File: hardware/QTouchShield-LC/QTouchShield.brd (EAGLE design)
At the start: 100 x 80 mm, 59 parts, among them IC1 AT32UC3C0512CJEDEC-MS-026, J1 SNS00...07, J10 CAPS08...15, J11 CAPS16...23, J12 CAPS24...31, J2 SNS08...15, J3 SNS16...23, J4 SNS24...31, J5 RES00...07, J6 RES08...15, J7 RES16...23, J8 RES24...31, J9 CAPS00...07, U1 ARDUINO-2560-MEGA-R3-SMD

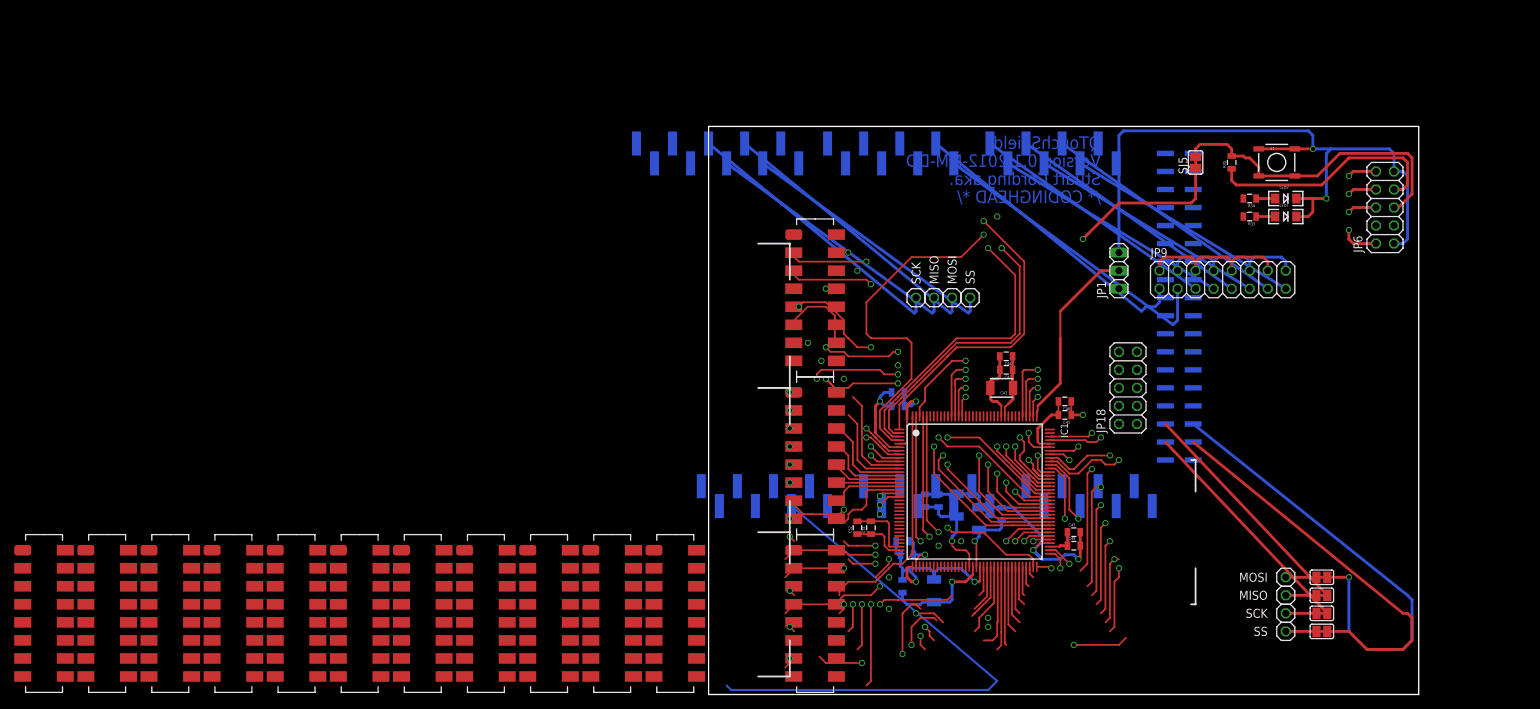
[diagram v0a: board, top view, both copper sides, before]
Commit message: Board ripped up - new surface mount headers fitted.
Ripped-up entire board. Most headers have been changed to surface mount
type.
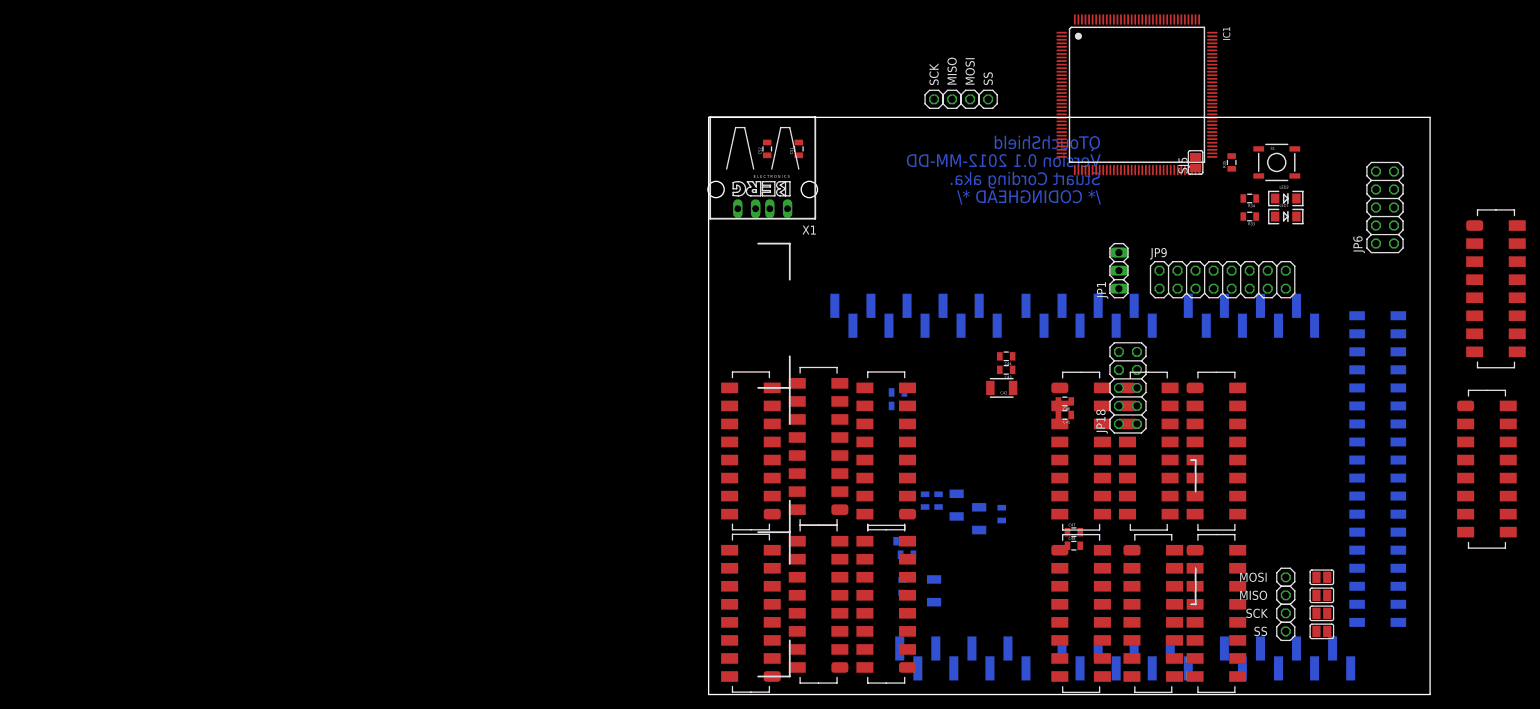
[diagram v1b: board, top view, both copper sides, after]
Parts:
- added X1: (no value), con-berg:PN87520
- moved J8 156.2 mm to (61.0, 20.3)
- moved J12 137.2 mm to (50.8, 20.3)
- moved U$2 132.6 mm to (109.2, 66.0)
- moved J11 130.3 mm to (50.8, 43.2)
- moved U$1 116.1 mm to (108.0, 40.6)
- moved J3 105.4 mm to (69.8, 43.2)
- moved J10 95.4 mm to (26.7, 25.4), turned to 180 degrees
- moved J4 94.0 mm to (69.8, 20.3)
- moved J9 87.9 mm to (26.7, 3.81), turned to 180 degrees
- moved J1 61.1 mm to (7.62, 2.54), turned to 180 degrees
- moved IC1 60.4 mm to (60.3, 84.5)
- moved C52 54.8 mm to (8.26, 76.8)
- moved C51 54.3 mm to (12.7, 76.8)
- moved J7 51.7 mm to (60.3, 43.2)
- moved J2 49.8 mm to (7.62, 25.4), turned to 180 degrees
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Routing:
- net GND: track 275.7 -> 0.00 mm, vias 7 -> 0
- net SDT-SPI0-SS: track 172.0 -> 0.00 mm, vias 1 -> 0
- net SDT-SPI0-MOSI: track 171.9 -> 0.00 mm, vias 2 -> 0
- net SDT-SPI0-SCK: track 150.4 -> 0.00 mm, vias 1 -> 0
- net SDT-SPI0-MISO: track 148.5 -> 0.00 mm, vias 1 -> 0
- net SNSK19: track 119.7 -> 0.00 mm, vias 5 -> 0
- net SNSK21: track 112.6 -> 0.00 mm, vias 3 -> 0
- net SNSK20: track 110.4 -> 0.00 mm, vias 4 -> 0
- net JTAG_RESET: track 109.4 -> 0.00 mm, vias 2 -> 0
- net JTAG_TCK: track 106.9 -> 0.00 mm, vias 2 -> 0
- net JTAG_TMS: track 105.9 -> 0.00 mm, vias 2 -> 0
- net JTAG_TDO: track 102.1 -> 0.00 mm, vias 3 -> 0
- net SNSK18: track 100.7 -> 0.00 mm, vias 4 -> 0
- net SNSK22: track 98.2 -> 0.00 mm, vias 5 -> 0
- net VCC: track 97.9 -> 0.00 mm, vias 5 -> 0
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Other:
- board size 100 x 80 mm -> 101.6 x 81.3 mm

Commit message: Major update to LC version of shield.
Major update to shield design including:
- Moving headers to surface mount technology
- Including level shifters for SPI and USART i/f
- USB connector for firmware flash upgrade (not yet complete)
- Jumper system for selecting MEGA or UNO style SPI interface
- Plus other tidying up
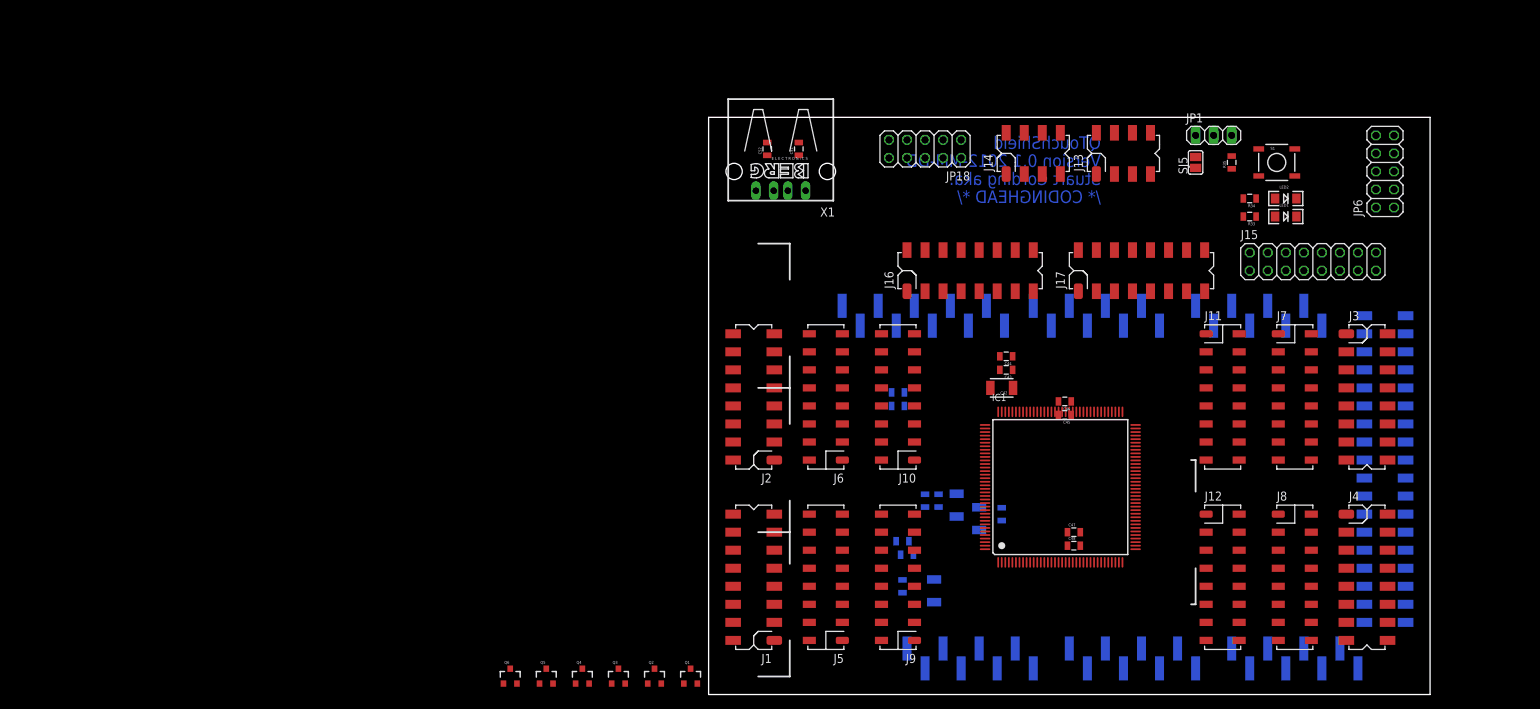
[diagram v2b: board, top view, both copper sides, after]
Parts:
- removed JP10, JP15: SS, pinhead:1X01
- removed JP11, JP14: SCK, pinhead:1X01
- removed JP12, JP17: MISO, pinhead:1X01
- removed JP13, JP16: MOSI, pinhead:1X01
- removed JP9: COMMS Select, pinhead:2X08
- removed SJ1, SJ2, SJ3, SJ4: (no value), jumper:SJ
- removed U$1, U$2: 2X8-HEADERSMD, codinghead:2X8-SOCKET-HEADER-SMD
- added J13: SPI-MEGA, codinghead:2X4-V-MALE-SMT-HARWIN
- added J14: SPI-UNO, codinghead:2X4-V-MALE-SMT-HARWIN
- added J15: COMMS Select, pinhead:2X08
- added J16: DETECT00...15, codinghead:2X8-V-MALE-SMT-HARWIN
- added J17: DETECT16...31, codinghead:2X8-V-MALE-SMT-HARWIN
- added Q1, Q2, Q3, Q4, Q5, Q6: BSS138, SparkFun:SOT23-3
- J1, J2, J3, J4: device codinghead:2X8-SOCKET-HEADER-SMD -> codinghead:2X8-V-MALE-SMT-HARWIN
- J10, J11, J12, J5, J6, J7, J8, J9: device codinghead:2X8-SOCKET-HEADER-SMD -> codinghead:2X8-V-FEMALE-SMT-HARWIN
- moved IC1 56.3 mm to (49.5, 29.2), turned to 0 degrees
- moved U1 46.0 mm to (96.5, 53.3)
- moved JP18 44.1 mm to (30.5, 76.8), turned to 180 degrees
- moved JP1 23.3 mm to (71.1, 78.7), turned to 0 degrees
- moved J3 22.9 mm to (91.4, 50.8)
- moved J7 22.3 mm to (81.3, 50.8)
- moved J4 22.2 mm to (91.4, 25.4)
- moved J11 21.7 mm to (71.1, 50.8)
- moved J12 20.9 mm to (71.1, 25.4)
- moved J8 20.9 mm to (81.3, 25.4)
- moved J10 7.73 mm to (27.9, 33.0)
- moved J2 7.62 mm to (7.62, 33.0)
- moved J6 7.01 mm to (17.8, 33.0)
- moved J1 5.08 mm to (7.62, 7.62)
- moved JP6 5.08 mm to (95.2, 73.7)
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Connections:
- new net ADT-SPI0-MISO: J13.2, J14.2, Q3.2
- new net ADT-SPI0-MOSI: J13.4, J14.4, Q4.2
- new net ADT-SPI0-SCK: J13.6, J14.6, Q2.2
- new net ADT-SPI0-SS: J13.8, J14.8, Q1.2
- new net ADT-USART0-RXD: J15.12, J15.16, J15.4, J15.8, Q5.2
- new net ADT-USART0-TXD: J15.10, J15.14, J15.2, J15.6, Q6.2
- new net IOREF: Q1.1, Q2.1, Q3.1, Q4.1, Q5.1, Q6.1, U1.IOREF
- new net MISO-MEGA: J13.1, U1.50
- new net MOSI-MEGA: J13.3, U1.51
- new net N$34: IC1.51, X1.3
- new net N$35: IC1.50, X1.2
- new net SCK-MEGA: J13.5, U1.52
- new net SS-MEGA: J13.7, U1.53
- net GND: now also X1.4
- net RX0: now also J15.3; no longer JP9.3
- net RX1: now also J15.15; no longer JP9.15
- net RX2: now also J15.11; no longer JP9.11
- net RX3: now also J15.7; no longer JP9.7
- net SDT-SPI0-MISO: now also Q3.3; no longer JP12.1, SJ4.1, SJ4.2, U1.50
- net SDT-SPI0-MOSI: now also Q4.3; no longer JP13.1, SJ3.1, SJ3.2, U1.51
- net SDT-SPI0-SCK: now also Q2.3; no longer JP11.1, SJ2.1, SJ2.2, U1.52
- net SDT-SPI0-SS: now also Q1.3; no longer JP10.1, SJ1.1, SJ1.2, U1.53
- net SDT-USART0-RXD: now also Q6.3; no longer JP9.12, JP9.16, JP9.4, JP9.8
- net SDT-USART0-TXD: now also Q5.3; no longer JP9.10, JP9.14, JP9.2, JP9.6
- net SHIELD-DETECT0: now also J16.1; no longer U$1.1
- net SHIELD-DETECT1: now also J16.2; no longer U$1.2
- net SHIELD-DETECT10: now also J16.11; no longer U$1.11
- net SHIELD-DETECT11: now also J16.12; no longer U$1.12
- net SHIELD-DETECT12: now also J16.13; no longer U$1.13
- net SHIELD-DETECT13: now also J16.14; no longer U$1.14
- net SHIELD-DETECT14: now also J16.15; no longer U$1.15
- net SHIELD-DETECT15: now also J16.16; no longer U$1.16
- net SHIELD-DETECT16: now also J17.1; no longer U$2.1
- net SHIELD-DETECT17: now also J17.2; no longer U$2.2
- net SHIELD-DETECT18: now also J17.3; no longer U$2.3
- net SHIELD-DETECT19: now also J17.4; no longer U$2.4
- net SHIELD-DETECT2: now also J16.3; no longer U$1.3
- net SHIELD-DETECT20: now also J17.5; no longer U$2.5
- net SHIELD-DETECT21: now also J17.6; no longer U$2.6
- net SHIELD-DETECT22: now also J17.7; no longer U$2.7
- net SHIELD-DETECT23: now also J17.8; no longer U$2.8
- net SHIELD-DETECT24: now also J17.9; no longer U$2.9
- net SHIELD-DETECT25: now also J17.10; no longer U$2.10
- net SHIELD-DETECT26: now also J17.11; no longer U$2.11
- net SHIELD-DETECT27: now also J17.12; no longer U$2.12
- net SHIELD-DETECT28: now also J17.13; no longer U$2.13
- net SHIELD-DETECT29: now also J17.14; no longer U$2.14
- net SHIELD-DETECT3: now also J16.4; no longer U$1.4
- net SHIELD-DETECT30: now also J17.15; no longer U$2.15
- net SHIELD-DETECT31: now also J17.16; no longer U$2.16
- net SHIELD-DETECT4: now also J16.5; no longer U$1.5
- net SHIELD-DETECT5: now also J16.6; no longer U$1.6
- net SHIELD-DETECT6: now also J16.7; no longer U$1.7
- net SHIELD-DETECT7: now also J16.8; no longer U$1.8
- net SHIELD-DETECT8: now also J16.9; no longer U$1.9
- net SHIELD-DETECT9: now also J16.10; no longer U$1.10
- net SPI-MISO-ALT: now also J14.1; no longer JP17.1
- net SPI-MOSI-ALT: now also J14.3; no longer JP16.1
- net SPI-SCK-ALT: now also J14.5; no longer JP14.1
- net SPI-SS-ALT: now also J14.7; no longer JP15.1
- net TX0: now also J15.1; no longer JP9.1
- net TX1: now also J15.13; no longer JP9.13
- net TX2: now also J15.9; no longer JP9.9
- net TX3: now also J15.5; no longer JP9.5

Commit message: Another attempt, more successful, at routingh the board!
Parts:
- removed JP18: TOUCH DATA, pinhead:2X05
- removed JP6: JTAG, pinhead:2X05
- added J18: JTAG, codinghead:2X5-V-MALE-THRUHOLE
- added J19: TOUCH DATA, codinghead:2X5-V-MALE-THRUHOLE
- J11: value CAPS16...23 -> CAPS24...31
- J12: value CAPS24...31 -> CAPS16...23
- X1: value (none) -> Firmware Upgrade Port
- moved Q6 117.9 mm to (71.1, 66.5)
- moved Q5 110.4 mm to (67.1, 66.5)
- moved Q4 103.1 mm to (63.0, 66.5)
- moved Q3 95.7 mm to (58.4, 66.5)
- moved Q2 88.7 mm to (53.8, 66.5)
- moved Q1 82.4 mm to (49.3, 66.5)
- moved C52 81.0 mm to (57.4, 12.5), turned to 180 degrees
- moved C51 79.8 mm to (57.4, 10.7), turned to 180 degrees
- moved C36 43.2 mm to (66.6, 33.3), flipped to the top, turned to 270 degrees
- moved C34 38.3 mm to (65.3, 17.1), flipped to the top, turned to 270 degrees
- moved C35 37.8 mm to (66.6, 29.3), flipped to the top
- moved C33 35.6 mm to (63.4, 17.1), flipped to the top, turned to 270 degrees
- moved C50 34.6 mm to (42.9, 12.0), flipped to the top
- moved C41 34.6 mm to (65.0, 24.9), flipped to the top, turned to 180 degrees
- moved C49 34.5 mm to (42.9, 10.2), flipped to the top
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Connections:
- net GND: now also J18.10, J18.2, J19.9; no longer JP18.9, JP6.10, JP6.2
- net JTAG_RESET: now also J18.6; no longer JP6.6
- net JTAG_TCK: now also J18.1; no longer JP6.1
- net JTAG_TDI: now also J18.9; no longer JP6.9
- net JTAG_TDO: now also J18.3; no longer JP6.3
- net JTAG_TMS: now also J18.5; no longer JP6.5
- net SNS16: now also J12.15; no longer J11.1
- net SNS17: now also J12.13; no longer J11.3
- net SNS18: now also J12.11; no longer J11.5
- net SNS19: now also J12.9; no longer J11.7
- net SNS20: now also J12.7; no longer J11.9
- net SNS21: now also J12.5; no longer J11.11
- net SNS22: now also J12.3; no longer J11.13
- net SNS23: now also J12.1; no longer J11.15
- net SNS24: now also J11.15; no longer J12.1
- net SNS25: now also J11.13; no longer J12.3
- net SNS26: now also J11.11; no longer J12.5
- net SNS27: now also J11.9; no longer J12.7
- net SNS28: now also J11.7; no longer J12.9
- net SNS29: now also J11.5; no longer J12.11
- net SNS30: now also J11.3; no longer J12.13
- net SNS31: now also J11.1; no longer J12.15
- net SNSK29: no longer J8.13
- net SNSK30: now also J8.13
- net TOUCH_DATA-MISO: now also J19.7; no longer JP18.7
- net TOUCH_DATA-MOSI: now also J19.6; no longer JP18.6
- net TOUCH_DATA-SCK: now also J19.8; no longer JP18.8
- net TOUCH_DATA-SS: now also J19.5; no longer JP18.5
- net VCC: now also J18.4, J19.10; no longer JP18.10, JP6.4
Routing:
- net GND: track 0.00 -> 359.4 mm, vias 0 -> 9
- net VCC: track 0.00 -> 213.7 mm, vias 0 -> 6
- net SNSK31: track 0.00 -> 116.7 mm, vias 0 -> 3
- net SNSK30: track 0.00 -> 106.9 mm, vias 0 -> 3
- net SNSK29: track 0.00 -> 99.6 mm, vias 0 -> 3
- net SNSK28: track 0.00 -> 95.3 mm, vias 0 -> 3
- net SNSK27: track 0.00 -> 91.4 mm, vias 0 -> 3
- net SNSK26: track 0.00 -> 87.5 mm, vias 0 -> 3
- net SNSK25: track 0.00 -> 83.6 mm, vias 0 -> 3
- net SNSK23: track 0.00 -> 81.7 mm, vias 0 -> 2
- net SNSK24: track 0.00 -> 78.3 mm, vias 0 -> 3
- net SNSK22: track 0.00 -> 76.5 mm, vias 0 -> 2
- net SNSK0: track 0.00 -> 76.4 mm, vias 0 -> 2
- net SNSK21: track 0.00 -> 71.8 mm, vias 0 -> 2
- net SNSK1: track 0.00 -> 71.3 mm, vias 0 -> 2
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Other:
- board text removed: "/* CODINGHEAD */"
- board text removed: "QTouchShield"
- board text removed: "Stuart Cording aka."
- board text removed: "Version 0.1 2012-MM-DD"
